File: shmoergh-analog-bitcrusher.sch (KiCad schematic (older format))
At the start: 36 parts, among them J2 Eurorack power, Q1 2N3819, U1 TL074, U2 TL072

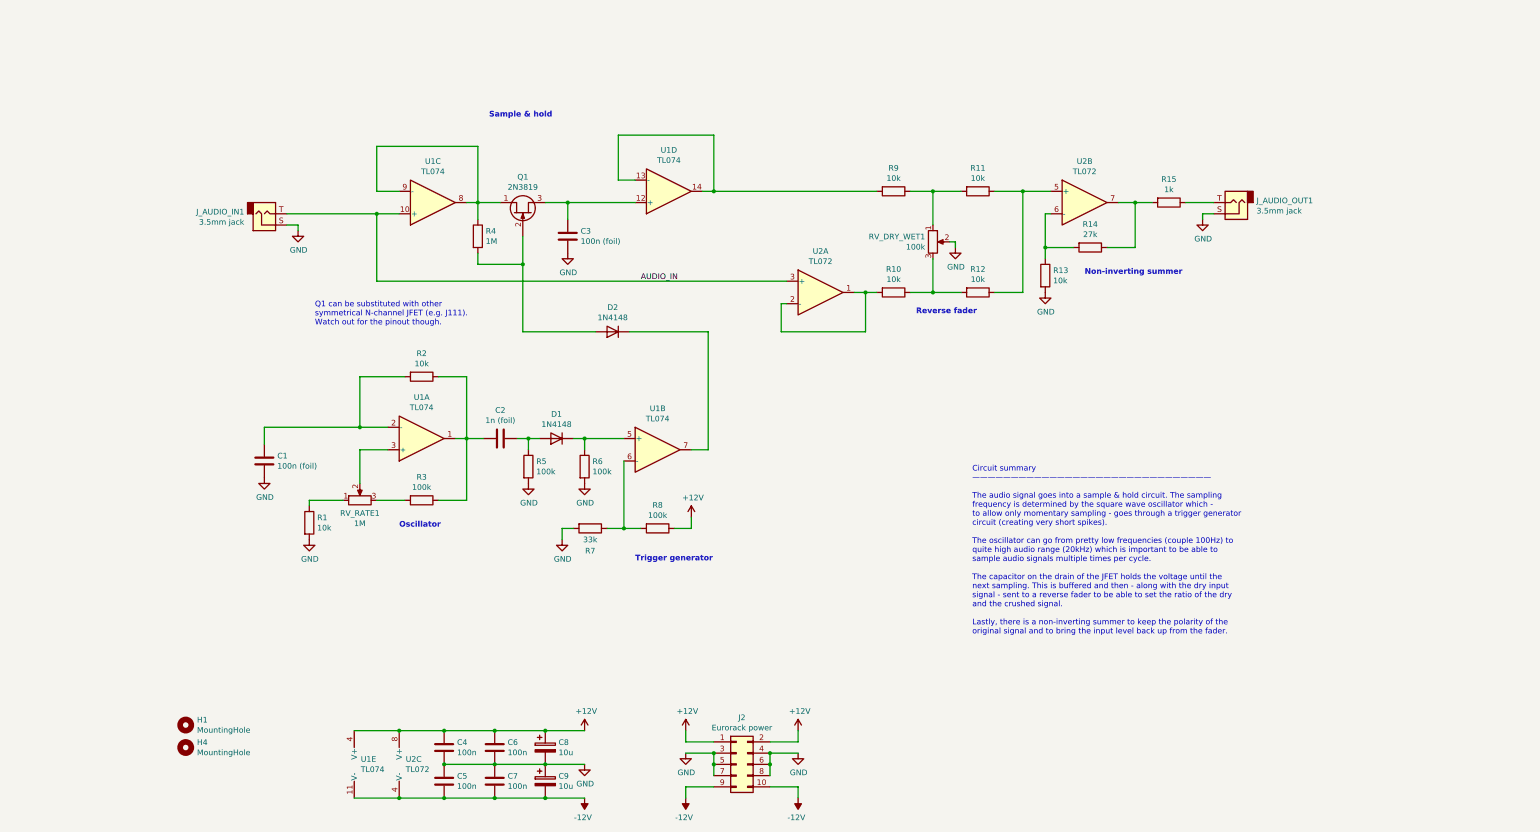
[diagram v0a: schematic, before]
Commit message: Added on/off switch to schematics
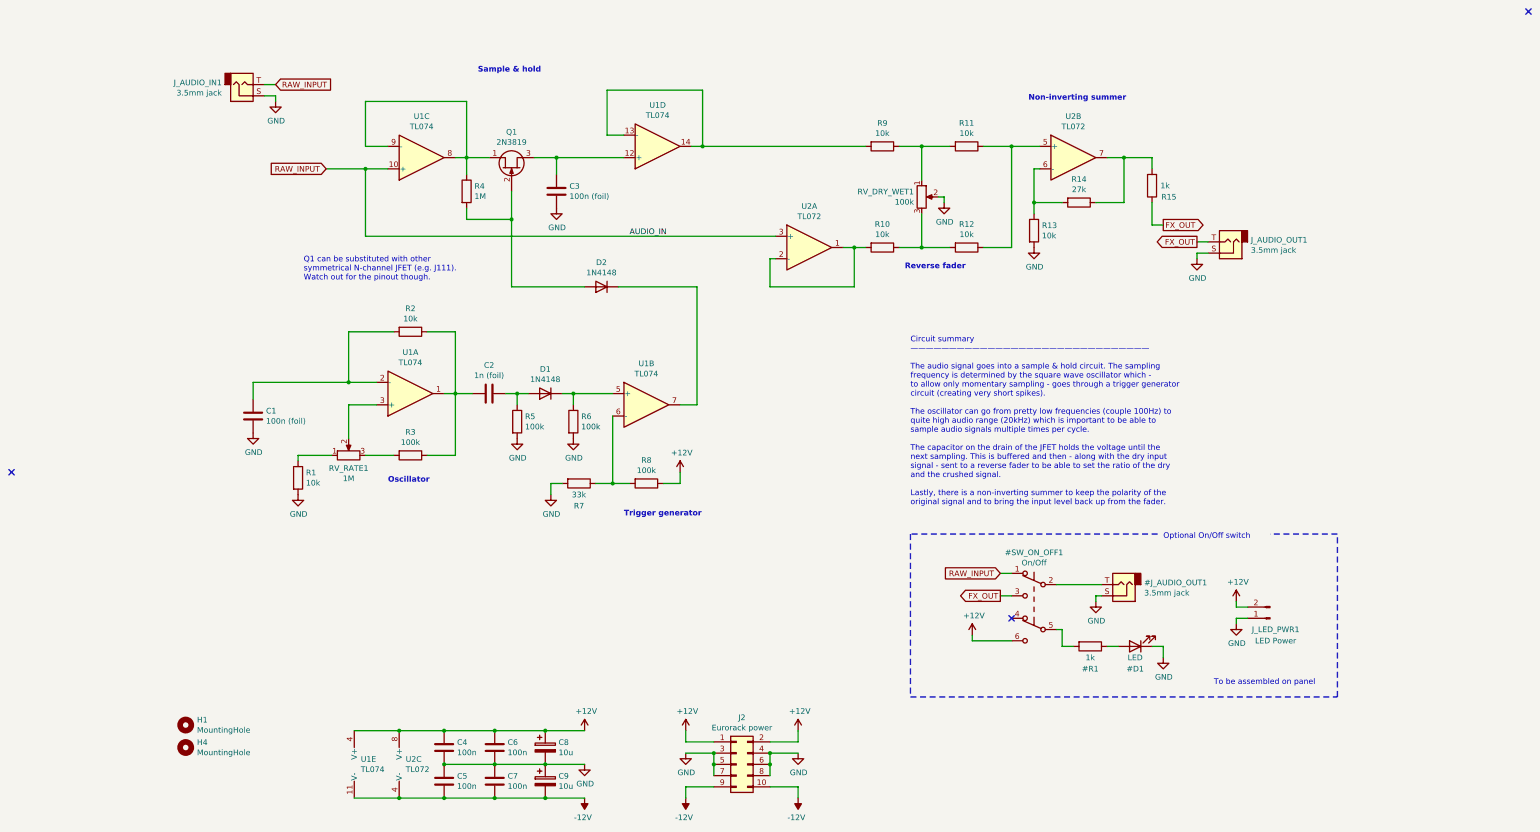
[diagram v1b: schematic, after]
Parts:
- added J_LED_PWR1: LED Power, Zimo_Manual_PCB:NSL25_01x02_Vertical, symbol Connector:Conn_01x02_Male
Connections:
- net +12V: now also J_LED_PWR1.2 (Pin_2)
- net GND: now also J_LED_PWR1.1 (Pin_1)
- net FX_OUT: now reaches J_AUDIO_OUT1.T, R15.1
- net AUDIO_IN renamed RAW_INPUT
- no-connect marks 0 -> 3
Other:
- note added: "Optional On/Off switch"
- note added: "To be assembled on panel"
- moved on the sheet: C1, C2, C3, D1, D2, J_AUDIO_IN1, J_AUDIO_OUT1, Q1, R1, R10, R11, R12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
